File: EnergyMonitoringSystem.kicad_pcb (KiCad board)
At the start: 4 copper layers, 0 parts

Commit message: pcb layout init
1. Pulled all items from schematics
2. Set board stackup and constraints
3. Create polygon pours for power and ground
4. Created isolated ground and power
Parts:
- added C201: 100n, Capacitor_SMD:C_0402_1005Metric, F.Cu at (99.7, 53.1)
- added C202: 100n, Capacitor_SMD:C_0402_1005Metric, F.Cu at (95.7, 48.9)
- added C203: 10u, Capacitor_SMD:C_0603_1608Metric, F.Cu at (108.0, 58.0)
- added C204: 10u, Capacitor_SMD:C_0603_1608Metric, F.Cu at (109.4, 52.6)
- added C301: 1u, Capacitor_SMD:C_0402_1005Metric, F.Cu at (115.2, 91.7)
- added C302: 1u, Capacitor_SMD:C_0402_1005Metric, F.Cu at (108.7, 93.0)
- added C303: 10u, Capacitor_SMD:C_0603_1608Metric, F.Cu at (97.1, 72.0)
- added C304: 47u, Capacitor_SMD:C_0603_1608Metric, F.Cu at (100.8, 72.0)
- added C305: 47u, Capacitor_SMD:C_0603_1608Metric, F.Cu at (101.3, 68.0)
- added C306: 10u, EMS:10SVPS10M, F.Cu at (125.5, 96.5)
- added C307: 10u, Capacitor_SMD:C_0603_1608Metric, F.Cu at (115.2, 67.8)
- added C308: 47u, Capacitor_SMD:C_0603_1608Metric, F.Cu at (109.9, 72.0)
- added C309: 47u, Capacitor_SMD:C_0603_1608Metric, F.Cu at (111.7, 63.2)
- added C310: 10u, EMS:10SVPS10M, F.Cu at (119.5, 104.5)
- added C401: 100n, Capacitor_SMD:C_0402_1005Metric, F.Cu at (132.8, 47.0)
- added C402: 100n, Capacitor_SMD:C_0402_1005Metric, F.Cu at (161.5, 65.2)
- added C403: 100n, Capacitor_SMD:C_0402_1005Metric, F.Cu at (157.0, 73.5)
- added C404: 100n, Capacitor_SMD:C_0402_1005Metric, F.Cu at (153.0, 70.0)
- added C405: 100n, Capacitor_SMD:C_0402_1005Metric, F.Cu at (146.2, 109.7)
- added C406: 100n, Capacitor_SMD:C_0402_1005Metric, F.Cu at (146.2, 113.2)
- added C407: 100n, Capacitor_SMD:C_0402_1005Metric, F.Cu at (157.0, 84.5)
- added C408: 2u2, Capacitor_SMD:C_0402_1005Metric, F.Cu at (155.0, 135.5)
- added C409: 100n, Capacitor_SMD:C_0402_1005Metric, F.Cu at (157.0, 135.5)
- added C410: 1u, Capacitor_SMD:C_0402_1005Metric, F.Cu at (154.5, 88.0)
- added C411: 1u, Capacitor_SMD:C_0402_1005Metric, F.Cu at (158.5, 91.0)
- added C412: 10n, Capacitor_SMD:C_0402_1005Metric, F.Cu at (154.5, 92.0)
- added C413: 100n, Capacitor_SMD:C_0402_1005Metric, F.Cu at (136.0, 136.5)
- added C414: 100n, Capacitor_SMD:C_0402_1005Metric, F.Cu at (142.0, 75.5)
- added C415: 100n, Capacitor_SMD:C_0402_1005Metric, F.Cu at (142.0, 82.5)
- added C416: 10u, Capacitor_SMD:C_0603_1608Metric, F.Cu at (139.0, 82.8)
- added C417: 6p8, Capacitor_SMD:C_0402_1005Metric, F.Cu at (151.0, 59.5)
- added C418: 5p6, Capacitor_SMD:C_0402_1005Metric, F.Cu at (159.3, 69.8)
- added C419: 100n, Capacitor_SMD:C_0402_1005Metric, F.Cu at (167.0, 81.5)
- added C420: 6p8, Capacitor_SMD:C_0402_1005Metric, F.Cu at (147.0, 63.5)
- added C421: 5p6, Capacitor_SMD:C_0402_1005Metric, F.Cu at (156.3, 65.5)
- added C501: 10p, Capacitor_SMD:C_0603_1608Metric, F.Cu at (72.5, 55.3)
- added C502: 6800p, Capacitor_SMD:C_0603_1608Metric, F.Cu at (75.5, 57.2)
- added C503: 10p, Capacitor_SMD:C_0603_1608Metric, F.Cu at (72.5, 58.8)
- added C504: 10p, Capacitor_SMD:C_0603_1608Metric, F.Cu at (72.2, 80.7)
- added C505: 6800p, Capacitor_SMD:C_0603_1608Metric, F.Cu at (74.8, 83.5)
- added C506: 10p, Capacitor_SMD:C_0603_1608Metric, F.Cu at (72.2, 85.7)
- added C507: 10p, Capacitor_SMD:C_0603_1608Metric, F.Cu at (72.2, 111.7)
- added C508: 6800p, Capacitor_SMD:C_0603_1608Metric, F.Cu at (74.5, 114.7)
- added C509: 10p, Capacitor_SMD:C_0603_1608Metric, F.Cu at (72.2, 116.7)
- added C510: 220n, Capacitor_SMD:C_0402_1005Metric, F.Cu at (93.8, 87.7)
- added C511: 1u, Capacitor_SMD:C_0402_1005Metric, F.Cu at (93.1, 89.7)
- added C512: 1u, Capacitor_SMD:C_0402_1005Metric, F.Cu at (100.3, 90.7)
- added C513: 10p, Capacitor_SMD:C_0603_1608Metric, F.Cu at (93.6, 84.9)
- added C514: 10p, Capacitor_SMD:C_0603_1608Metric, F.Cu at (89.2, 110.5)
- added C515: 6800p, Capacitor_SMD:C_0603_1608Metric, F.Cu at (92.8, 110.5)
- added C516: 10p, Capacitor_SMD:C_0603_1608Metric, F.Cu at (108.5, 110.5)
- added C517: 6800p, Capacitor_SMD:C_0603_1608Metric, F.Cu at (112.0, 110.5)
- added C518: 10p, Capacitor_SMD:C_0603_1608Metric, F.Cu at (127.0, 110.5)
- added C519: 6800p, Capacitor_SMD:C_0603_1608Metric, F.Cu at (130.7, 110.5)
- added C601: 100n, Capacitor_SMD:C_0402_1005Metric, F.Cu at (167.5, 128.2)
- added C602: 100n, Capacitor_SMD:C_0402_1005Metric, F.Cu at (164.8, 128.0)
- added C603: 10u, Capacitor_SMD:C_0603_1608Metric, F.Cu at (169.0, 96.0)
- added C604: 0.1u, Capacitor_SMD:C_0402_1005Metric, F.Cu at (166.0, 102.5)
- added C605: 0.1u, Capacitor_SMD:C_0402_1005Metric, F.Cu at (183.0, 116.5)
- added C606: 10u, Capacitor_SMD:C_0603_1608Metric, F.Cu at (181.0, 112.0)
- added C607: 10u, Capacitor_SMD:C_0603_1608Metric, F.Cu at (169.0, 107.0)
- added C608: 0.1u, Capacitor_SMD:C_0402_1005Metric, F.Cu at (163.0, 97.5)
- added C609: 0.1u, Capacitor_SMD:C_0402_1005Metric, F.Cu at (186.0, 111.5)
- added D201: BAT30KFILM, EMS:BAT30KFILM, F.Cu at (96.6, 46.2)
- added D202: ESDA7P60-1U1M, EMS:ESDA7P60-1U1M, F.Cu at (92.3, 46.7)
- added D401: ESDALC6V1-1M2, EMS:ESDALC6V11M2, F.Cu at (152.9, 51.8)
- added D402: ESDALC6V1-1M2, EMS:ESDALC6V11M2, F.Cu at (135.5, 51.0)
- added D403: PESD3V3L1BA,115, EMS:PESD3V3L1BA_115-SOD-323-2, F.Cu at (168.5, 58.5)
- added D404: PESD3V3L1BA,115, EMS:PESD3V3L1BA_115-SOD-323-2, F.Cu at (179.7, 57.3)
- added D405: PESD3V3L1BA,115, EMS:PESD3V3L1BA_115-SOD-323-2, F.Cu at (180.0, 63.3)
- added D406: PESD3V3L1BA,115, EMS:PESD3V3L1BA_115-SOD-323-2, F.Cu at (183.7, 60.8)
- added D407: PESD3V3L1BA,115, EMS:PESD3V3L1BA_115-SOD-323-2, F.Cu at (183.7, 54.6)
- added D408: LED_RAGB, LED_SMD:LED_Kingbright_APFA3010_3x1.5mm_Horizontal, F.Cu at (169.0, 78.5)
- added FB601: FerriteBead, EMS:BLM15HD182SN1D, F.Cu at (180.0, 118.4)
- added FB602: FerriteBead, EMS:BLM15HD182SN1D, F.Cu at (187.0, 106.4)
- added J201: USB_C_Receptacle_USB2.0_16P, Connector_USB:USB_C_Receptacle_GCT_USB4105-xx-A_16P_TopMnt_Horizontal, F.Cu at (103.5, 41.3)
- added J202: Screw_Terminal_01x02, TerminalBlock_Phoenix:TerminalBlock_Phoenix_MKDS-1,5-2-5.08_1x02_P5.08mm_Horizontal, F.Cu at (121.0, 42.1)
- added J401: Conn_02x05_Counter_Clockwise, EMS:62701021621, F.Cu at (172.7, 55.9)
- added J402: Conn_02x05_Counter_Clockwise, EMS:62701021621, F.Cu at (152.7, 120.9)
- added J403: Conn_02x08_Counter_Clockwise, Connector_PinHeader_2.54mm:PinHeader_2x10_P2.54mm_Vertical, F.Cu at (141.2, 101.0)
- added J501: Screw_Terminal_01x02, TerminalBlock_Phoenix:TerminalBlock_Phoenix_MKDS-1,5-2-5.08_1x02_P5.08mm_Horizontal, F.Cu at (35.5, 56.9)
- added J502: Screw_Terminal_01x02, TerminalBlock_Phoenix:TerminalBlock_Phoenix_MKDS-1,5-2-5.08_1x02_P5.08mm_Horizontal, F.Cu at (35.5, 85.8)
- added J503: Screw_Terminal_01x02, TerminalBlock_Phoenix:TerminalBlock_Phoenix_MKDS-1,5-2-5.08_1x02_P5.08mm_Horizontal, F.Cu at (35.5, 114.4)
- added J504: Screw_Terminal_01x02, TerminalBlock_Phoenix:TerminalBlock_Phoenix_MKDS-1,5-2-5.08_1x02_P5.08mm_Horizontal, F.Cu at (84.9, 144.0)
- added J505: Screw_Terminal_01x02, TerminalBlock_Phoenix:TerminalBlock_Phoenix_MKDS-1,5-2-5.08_1x02_P5.08mm_Horizontal, F.Cu at (104.5, 144.0)
- added J506: Screw_Terminal_01x02, TerminalBlock_Phoenix:TerminalBlock_Phoenix_MKDS-1,5-2-5.08_1x02_P5.08mm_Horizontal, F.Cu at (123.9, 144.0)
- added J601: DM3AT-SF-PEJM5_40_, EMS:DM3ATSFPEJM540, F.Cu at (169.6, 133.0)
- added J602: Screw_Terminal_01x03, TerminalBlock_Phoenix:TerminalBlock_Phoenix_MKDS-1,5-3-5.08_1x03_P5.08mm_Horizontal, F.Cu at (195.0, 110.0)
- added L301: 2u2, Inductor_SMD:L_0603_1608Metric, F.Cu at (93.8, 67.5)
- added L302: 10u, Inductor_SMD:L_0805_2012Metric, F.Cu at (93.8, 63.7)
- added L303: 2u2, Inductor_SMD:L_0603_1608Metric, F.Cu at (108.0, 68.0)
- added L304: 10u, Inductor_SMD:L_0805_2012Metric, F.Cu at (108.0, 64.2)
- added L401: 10n, Inductor_SMD:L_0603_1608Metric, F.Cu at (158.2, 88.0)
- added Q201: STL6N3LLH6, EMS:STL6N3LLH6, F.Cu at (101.1, 54.9)
- added R201: 10k, Resistor_SMD:R_0603_1608Metric, F.Cu at (103.4, 48.1)
- added R202: 120R, Resistor_SMD:R_0402_1005Metric, F.Cu at (112.1, 56.3)
- added R203: 2k7, Resistor_SMD:R_0603_1608Metric, F.Cu at (103.4, 51.8)
- added R301: 100k, Resistor_SMD:R_0603_1608Metric, F.Cu at (114.4, 88.2)
- added R302: 100k, Resistor_SMD:R_0603_1608Metric, F.Cu at (115.3, 70.8)
- added R401: 49R9, Resistor_SMD:R_0402_1005Metric, F.Cu at (171.5, 49.9)
- added R402: 49R9, Resistor_SMD:R_0402_1005Metric, F.Cu at (175.2, 49.9)
- added R403: 49R9, Resistor_SMD:R_0402_1005Metric, F.Cu at (171.2, 46.7)
- added R404: 49R9, Resistor_SMD:R_0402_1005Metric, F.Cu at (175.2, 46.7)
- added R405: 10k, Resistor_SMD:R_0603_1608Metric, F.Cu at (149.4, 46.2)
- added R406: 47k, Resistor_SMD:R_0603_1608Metric, F.Cu at (136.0, 140.8)
- added R407: 47k, Resistor_SMD:R_0603_1608Metric, F.Cu at (157.0, 141.2)
- added R408: 1k, Resistor_SMD:R_0603_1608Metric, F.Cu at (165.1, 80.0)
- added R409: 1k, Resistor_SMD:R_0603_1608Metric, F.Cu at (165.1, 78.5)
- added R410: 1k, Resistor_SMD:R_0603_1608Metric, F.Cu at (165.1, 77.0)
- added R501: 330k, Resistor_SMD:R_0805_2012Metric, F.Cu at (57.4, 54.5)
- added R502: 330k, Resistor_SMD:R_0805_2012Metric, F.Cu at (61.4, 54.5)
- added R503: 330k, Resistor_SMD:R_0805_2012Metric, F.Cu at (65.3, 54.5)
- added R504: 1k, Resistor_SMD:R_0603_1608Metric, F.Cu at (69.2, 54.5)
- added R505: R_Variable, EMS:B72220S0271K101, F.Cu at (52.0, 54.5)
- added R506: 750R, Resistor_SMD:R_0805_2012Metric, F.Cu at (65.2, 58.1)
- added R507: 1k, Resistor_SMD:R_0603_1608Metric, F.Cu at (69.2, 59.0)
- added R508: 330k, Resistor_SMD:R_0805_2012Metric, F.Cu at (57.1, 80.0)
- added R509: 330k, Resistor_SMD:R_0805_2012Metric, F.Cu at (61.1, 80.0)
- added R510: 330k, Resistor_SMD:R_0805_2012Metric, F.Cu at (65.1, 80.0)
- added R511: 1k, Resistor_SMD:R_0603_1608Metric, F.Cu at (68.9, 80.0)
- added R512: R_Variable, EMS:B72220S0271K101, F.Cu at (52.0, 82.5)
- added R513: 750R, Resistor_SMD:R_0805_2012Metric, F.Cu at (65.0, 84.1)
- added R514: 1k, Resistor_SMD:R_0603_1608Metric, F.Cu at (68.9, 85.0)
- added R515: 330k, Resistor_SMD:R_0805_2012Metric, F.Cu at (56.9, 111.0)
- added R516: 330k, Resistor_SMD:R_0805_2012Metric, F.Cu at (61.0, 111.0)
- added R517: 330k, Resistor_SMD:R_0805_2012Metric, F.Cu at (65.0, 111.0)
- added R518: 1k, Resistor_SMD:R_0603_1608Metric, F.Cu at (69.0, 111.0)
- added R519: R_Variable, EMS:B72220S0271K101, F.Cu at (52.0, 111.0)
- added R520: 750R, Resistor_SMD:R_0805_2012Metric, F.Cu at (64.8, 115.1)
- added R521: 1k, Resistor_SMD:R_0603_1608Metric, F.Cu at (69.0, 116.0)
- added R522: 33R, Resistor_SMD:R_0603_1608Metric, F.Cu at (94.4, 82.1)
- added R523: 33R, Resistor_SMD:R_0603_1608Metric, F.Cu at (96.3, 83.5)
- added R524: 7k15, Resistor_SMD:R_0603_1608Metric, F.Cu at (89.0, 134.5)
- added R525: 33R, Resistor_SMD:R_0603_1608Metric, F.Cu at (98.0, 83.5)
- added R526: 10k, Resistor_SMD:R_0603_1608Metric, F.Cu at (103.7, 82.7)
- added R527: 33R, Resistor_SMD:R_0603_1608Metric, F.Cu at (99.6, 83.5)
- added R528: 100k, Resistor_SMD:R_0603_1608Metric, F.Cu at (98.9, 86.0)
- added R529: 33R, Resistor_SMD:R_0603_1608Metric, F.Cu at (101.2, 83.5)
- added R530: 100k, Resistor_SMD:R_0603_1608Metric, F.Cu at (107.5, 86.0)
- added R531: 1k, Resistor_SMD:R_0603_1608Metric, F.Cu at (88.2, 131.6)
- added R532: 2k, Resistor_SMD:R_0603_1608Metric, F.Cu at (90.8, 114.0)
- added R533: 33R, Resistor_SMD:R_0603_1608Metric, F.Cu at (104.1, 89.8)
- added R534: 100k, Resistor_SMD:R_0603_1608Metric, F.Cu at (84.8, 133.6)
- added R535: 100k, Resistor_SMD:R_0603_1608Metric, F.Cu at (80.9, 128.5)
- added R536: 62k, Resistor_SMD:R_0603_1608Metric, F.Cu at (90.8, 117.2)
- added R537: 100k, Resistor_SMD:R_0603_1608Metric, F.Cu at (85.6, 130.8)
- added R538: 10k, Resistor_SMD:R_0603_1608Metric, F.Cu at (86.6, 117.2)
- added R539: 100k, Resistor_SMD:R_0603_1608Metric, F.Cu at (92.9, 129.0)
- added R540: 7k15, Resistor_SMD:R_0603_1608Metric, F.Cu at (103.7, 131.8)
- added R541: 1k, Resistor_SMD:R_0603_1608Metric, F.Cu at (108.2, 131.8)
- added R542: 2k, Resistor_SMD:R_0603_1608Metric, F.Cu at (110.1, 113.8)
- added R543: 100k, Resistor_SMD:R_0603_1608Metric, F.Cu at (104.5, 134.9)
- added R544: 100k, Resistor_SMD:R_0603_1608Metric, F.Cu at (103.7, 129.0)
- added R545: 62k, Resistor_SMD:R_0603_1608Metric, F.Cu at (110.1, 117.2)
- added R546: 100k, Resistor_SMD:R_0603_1608Metric, F.Cu at (108.3, 135.5)
- added R547: 10k, Resistor_SMD:R_0603_1608Metric, F.Cu at (103.6, 117.2)
- added R548: 100k, Resistor_SMD:R_0603_1608Metric, F.Cu at (110.9, 129.0)
- added R549: 7k15, Resistor_SMD:R_0603_1608Metric, F.Cu at (123.2, 131.8)
- added R550: 1k, Resistor_SMD:R_0603_1608Metric, F.Cu at (128.2, 131.8)
- added R551: 2k, Resistor_SMD:R_0603_1608Metric, F.Cu at (128.7, 113.5)
- added R552: 100k, Resistor_SMD:R_0603_1608Metric, F.Cu at (123.5, 135.1)
- added R553: 100k, Resistor_SMD:R_0603_1608Metric, F.Cu at (123.1, 129.0)
- added R554: 62k, Resistor_SMD:R_0603_1608Metric, F.Cu at (129.3, 117.5)
- added R555: 100k, Resistor_SMD:R_0603_1608Metric, F.Cu at (128.3, 136.0)
- added R556: 10k, Resistor_SMD:R_0603_1608Metric, F.Cu at (123.3, 117.5)
- added R557: 100k, Resistor_SMD:R_0603_1608Metric, F.Cu at (130.8, 129.0)
- added R601: 120R, Resistor_SMD:R_0402_1005Metric, F.Cu at (183.0, 121.0)
- added SW401: SW_Push, Button_Switch_SMD:SW_SPST_CK_RS282G05A3, F.Cu at (139.0, 47.0)
- added SW402: SW_Push, Button_Switch_SMD:SW_SPST_CK_RS282G05A3, F.Cu at (155.9, 47.0)
- added TP201: TestPoint, EMS:5000, F.Cu at (85.0, 56.0)
- added TP202: TestPoint, EMS:5000, F.Cu at (85.0, 64.0)
- added TP301: TestPoint, EMS:5000, F.Cu at (64.8, 145.0)
- added TP302: TestPoint, EMS:5000, F.Cu at (64.8, 131.8)
- added TP303: TestPoint, EMS:5000, F.Cu at (64.8, 135.5)
- added TP304: TestPoint, EMS:5000, F.Cu at (64.8, 139.2)
- added TP601: TestPoint, EMS:5000, F.Cu at (187.0, 92.0)
- added TP602: TestPoint, EMS:5000, F.Cu at (182.0, 130.0)
- added TP603: TestPoint, EMS:5000, F.Cu at (173.0, 92.0)
- added U201: USBLC6-2P6, EMS:USBLC62P6-SOT666-6, F.Cu at (108.1, 49.1)
- added U202: STEF05SGR, EMS:STEF05SGR-TSOT23-8L, F.Cu at (108.6, 55.4)
- added U203: TCPP01-M12, EMS:TCPP01-M12-QFN-12L, F.Cu at (98.7, 50.2)
- added U301: LDLN025M12R, EMS:LDLN025M12R-SOT-23-5, F.Cu at (112.2, 91.2)
- added U302: ST1PS02CQTR, EMS:ST1PS02CQTR, F.Cu at (97.6, 67.5)
- added U303: ST1PS02CQTR, EMS:ST1PS02CQTR, F.Cu at (111.7, 67.6)
- added U304: LM2664M6_NOPB, EMS:LM2664M6_NOPB-SOT-23-6, F.Cu at (125.8, 102.0)
- added U401: STM32F103RGT6, EMS:STM32F103RGT6-LQFP-64, F.Cu at (149.5, 78.8)
- added U402: BLUENRG-M2SA, EMS:BLUENRG-M2SA, F.Cu at (146.5, 145.2)
- added U501: ADS131M08IRSNR, EMS:ADS131M08IPBS-WQFN-A, F.Cu at (96.6, 91.2)
- added U502: TSV914AIDR, EMS:TSV914AIDR-SOIC-14, F.Cu at (87.5, 123.4)
- added U503: TSV914AIDR, EMS:TSV914AIDR-SOIC-14, F.Cu at (106.8, 123.4)
- added U504: TSV914AIDR, EMS:TSV914AIDR-SOIC-14, F.Cu at (126.2, 123.5)
- added U601: EMIF06-MSD02N16, EMS:EMIF06-MSD02N16, F.Cu at (160.3, 122.2)
- added U602: ADM2565EBRNZ, EMS:ADM2565EBRNZ-SOIC-28, F.Cu at (178.6, 103.2)
- added Y401: 16MHz, Crystal:Crystal_SMD_3225-4Pin_3.2x2.5mm, F.Cu at (151.1, 63.1)
- added Y402: 32.768KHz, Crystal:Crystal_SMD_3215-2Pin_3.2x1.5mm, F.Cu at (157.0, 67.5)
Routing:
- added copper zone on In3.Cu, net +DCDC_1
- added copper zone on In3.Cu, net +V_ISO
- added copper zone on In1.Cu, net GND
- added copper zone on In4.Cu, net GND
- added copper zone on In1.Cu, net GND2
- added copper zone on In4.Cu, net GND2
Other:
- board outline added: 170 x 117 mm
- copper layers 4 -> 6

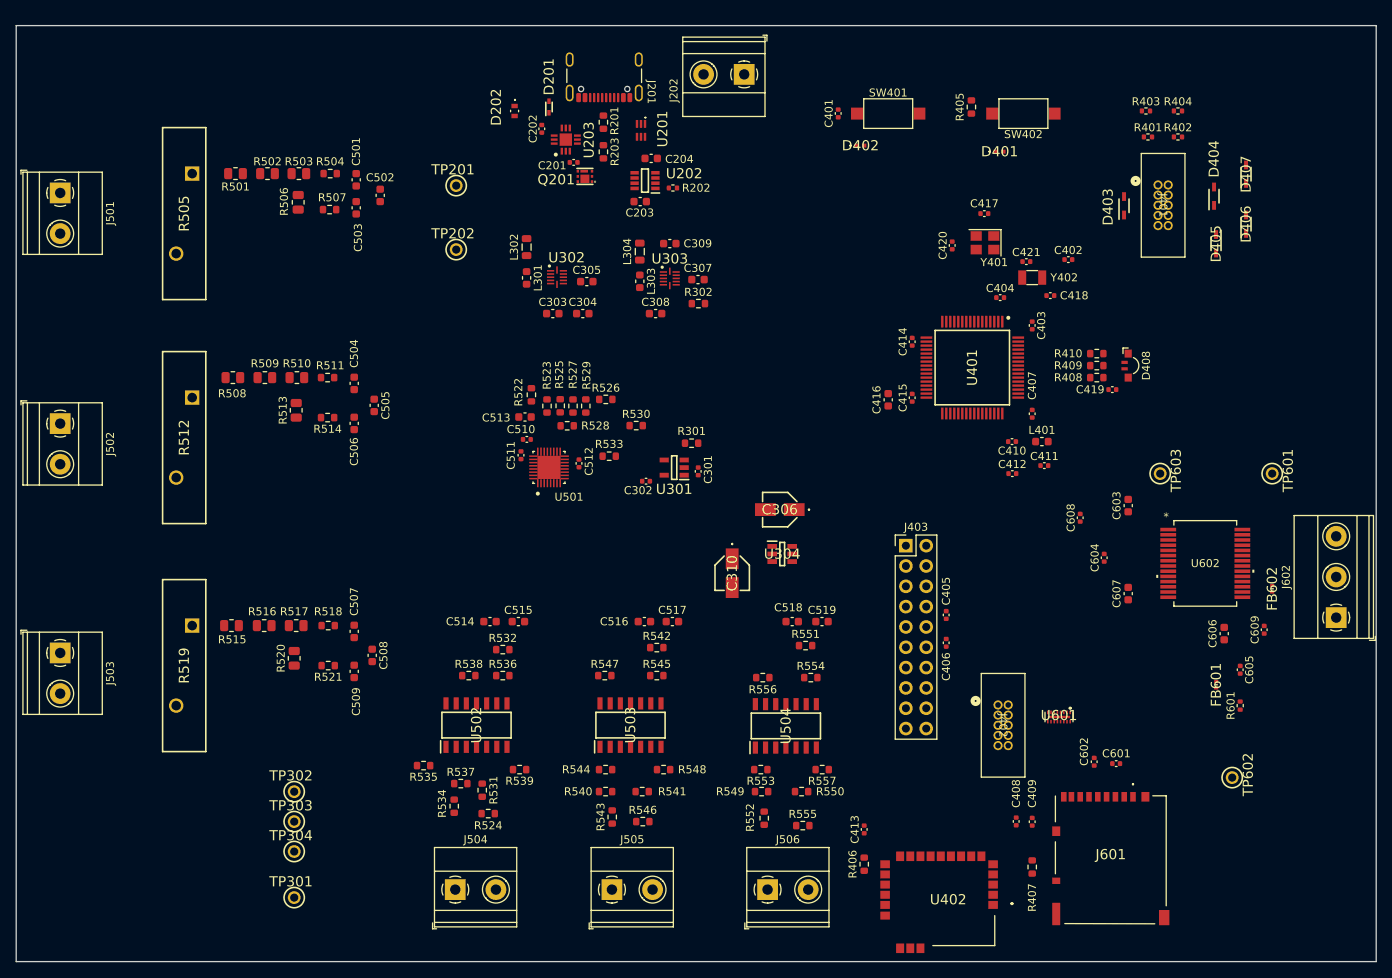
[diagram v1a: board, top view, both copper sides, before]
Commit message: routed board power supply
1. USB
2. LDO for DCDC_1 and DCDC_2
3. LDO for +1V2
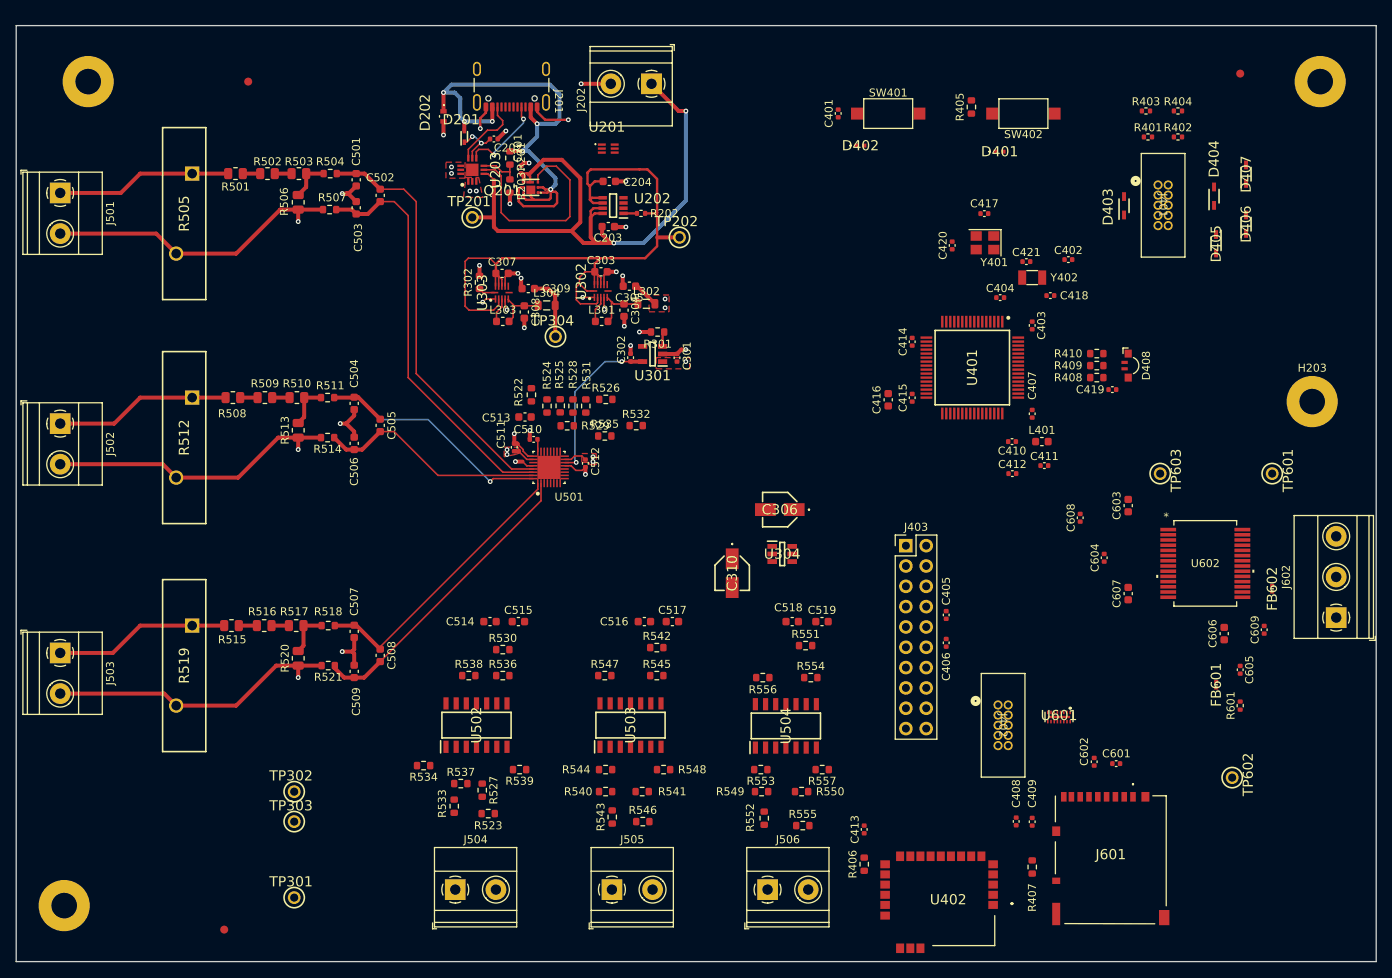
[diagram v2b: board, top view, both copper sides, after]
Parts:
- added FM201: Fiducial, Fiducial:Fiducial_1mm_Mask2mm, F.Cu at (59.0, 43.0)
- added FM202: Fiducial, Fiducial:Fiducial_1mm_Mask2mm, F.Cu at (183.0, 42.0)
- added FM203: Fiducial, Fiducial:Fiducial_1mm_Mask2mm, F.Cu at (56.0, 149.0)
- added H201: MountingHole_Pad, MountingHole:MountingHole_3.2mm_M3_Pad, F.Cu at (39.0, 43.0)
- added H202: MountingHole_Pad, MountingHole:MountingHole_3.2mm_M3_Pad, F.Cu at (193.0, 43.0)
- added H203: MountingHole_Pad, MountingHole:MountingHole_3.2mm_M3_Pad, F.Cu at (192.0, 83.0)
- added H204: MountingHole_Pad, MountingHole:MountingHole_3.2mm_M3_Pad, F.Cu at (36.0, 146.0)
- moved TP304 72.2 mm to (97.4, 74.9)
- moved TP202 28.0 mm to (112.9, 62.5)
- moved R302 27.5 mm to (87.9, 68.1), turned to 90 degrees
- moved C307 24.5 mm to (90.7, 67.0)
- moved U303 21.1 mm to (90.7, 69.4), turned to 90 degrees
- moved C309 18.6 mm to (94.0, 68.9)
- moved L303 17.8 mm to (90.8, 73.0), turned to 0 degrees
- moved L302 16.6 mm to (108.8, 70.8), turned to 0 degrees
- moved C308 16.4 mm to (93.5, 71.8), turned to -90 degrees
- moved C302 15.6 mm to (106.8, 77.5), turned to 90 degrees
- moved R301 14.5 mm to (110.2, 74.3), turned to 0 degrees
- moved U301 14.5 mm to (109.5, 77.0)
- moved C301 14.4 mm to (112.6, 77.5)
- moved L304 13.4 mm to (96.3, 71.0), turned to 0 degrees
- moved R201 12.5 mm to (91.7, 52.5)
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- renumbered R524 to R523, R523 to R524, R531 to R527, R527 to R528, R528 to R529, R532 to R530, R529 to R531, R530 to R532, R534 to R533, R535 to R534, R533 to R535
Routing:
- net GND: track 0.00 -> 181.1 mm, vias 0 -> 37
- net +5V: track 0.00 -> 92.0 mm
- net +5V_EXT: track 0.00 -> 83.1 mm, vias 0 -> 2
- net +VBUSc: track 0.00 -> 71.1 mm, vias 0 -> 6
- net /ADC/V_Phase_A_P: track 0.00 -> 52.4 mm
- net /ADC/V_Phase_A_N: track 0.00 -> 51.4 mm
- net /ADC/V_Phase_C_N: track 0.00 -> 37.9 mm
- net /ADC/V_Phase_C_P: track 0.00 -> 35.8 mm
- net /ADC/V_Phase_B_P: track 0.00 -> 29.4 mm, vias 0 -> 1
- net /ADC/V_Phase_B_N: track 0.00 -> 28.7 mm
- net /USB/PD_GATE: track 0.00 -> 26.9 mm
- net Net-(J502-Pin_1): track 0.00 -> 22.0 mm
- net Net-(J501-Pin_1): track 0.00 -> 22.0 mm
- net Net-(J503-Pin_1): track 0.00 -> 21.9 mm
- net +1V2: track 0.00 -> 20.4 mm, vias 0 -> 2
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- added copper zone on F.Cu, net +DCDC_1
- added copper zone on F.Cu, net GND

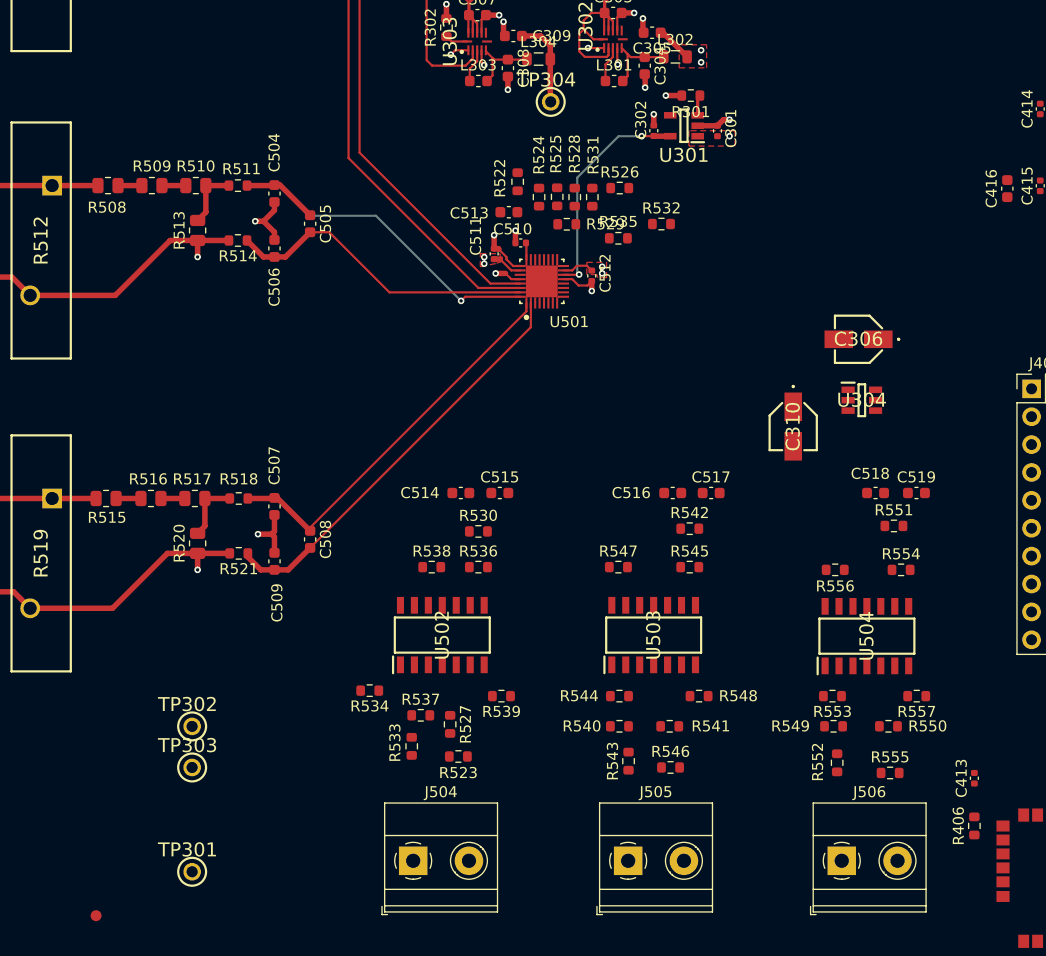
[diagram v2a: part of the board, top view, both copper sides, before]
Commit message: routing of CTs complete
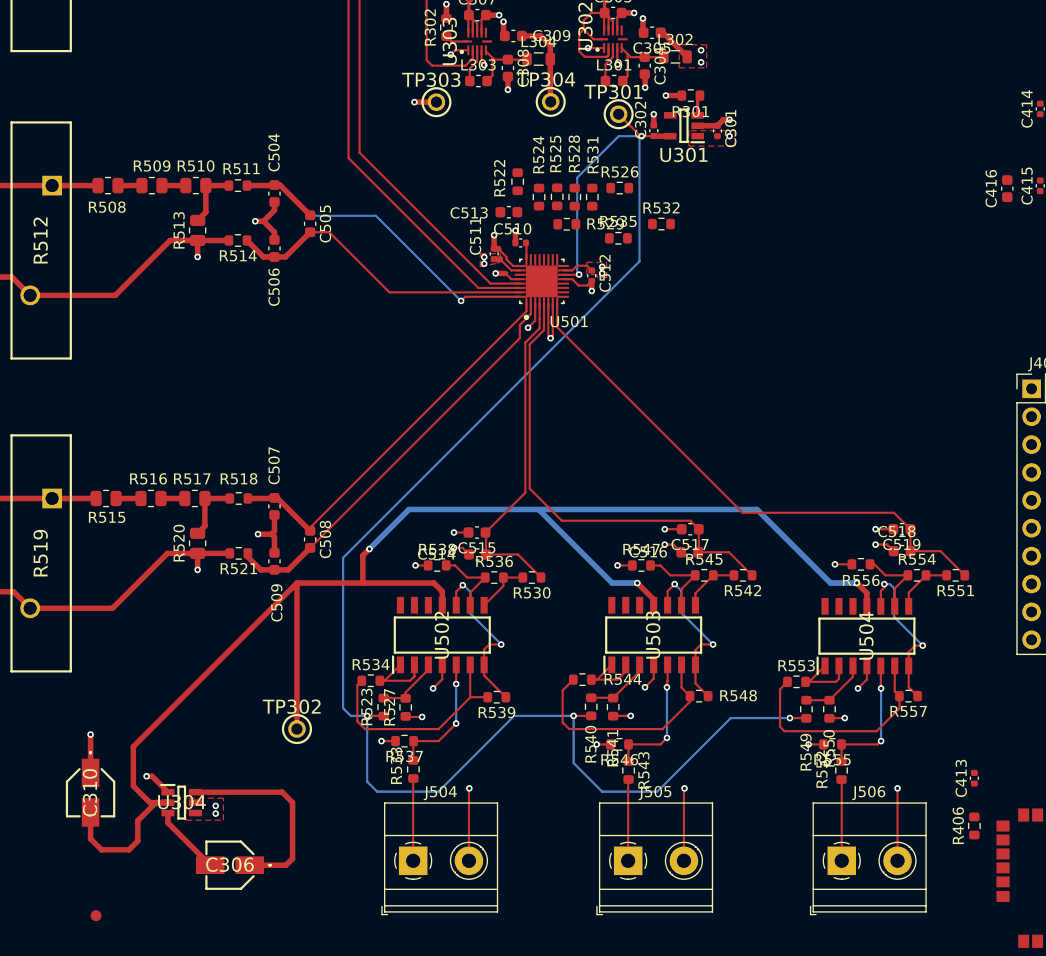
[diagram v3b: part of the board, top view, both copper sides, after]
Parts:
- moved TP301 79.2 mm to (103.6, 76.0)
- moved C306 74.6 mm to (68.2, 144.4)
- moved C310 72.2 mm to (55.5, 137.8)
- moved U304 72.0 mm to (63.8, 138.7)
- moved TP303 64.6 mm to (87.0, 74.9)
- moved TP302 9.55 mm to (74.3, 132.0)
- moved R523 8.15 mm to (82.2, 130.0), turned to -90 degrees
- moved R551 7.20 mm to (134.3, 118.0), turned to 180 degrees
- moved R542 6.45 mm to (114.9, 118.0), turned to 180 degrees
- moved R530 6.43 mm to (95.7, 118.2), turned to 180 degrees
- moved R555 5.86 mm to (123.1, 133.4), turned to 180 degrees
- moved C518 5.83 mm to (129.4, 115.8)
- moved C514 5.80 mm to (90.8, 116.1)
- moved C516 5.62 mm to (110.1, 115.9)
- moved R550 5.59 mm to (122.8, 130.2), turned to 90 degrees
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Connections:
- R534 pad 2: /ADC/VB_REF -> /ADC/VB_REF_A
- R539 pad 1: /ADC/LS_REF -> /ADC/LS_REF_A
- R544 pad 2: /ADC/VB_REF -> /ADC/VB_REF_B
- R548 pad 1: /ADC/LS_REF -> /ADC/LS_REF_B
- R553 pad 2: /ADC/VB_REF -> /ADC/VB_REF_C
- R557 pad 1: /ADC/LS_REF -> /ADC/LS_REF_C
- U502 pad 1: /ADC/VB_REF -> /ADC/VB_REF_A
- U502 pad 10: /ADC/LS_REF -> /ADC/LS_REF_A
- U502 pad 2: /ADC/VB_REF -> /ADC/VB_REF_A
- U502 pad 7: /ADC/LS_REF -> /ADC/LS_REF_A
- U503 pad 1: /ADC/VB_REF -> /ADC/VB_REF_B
- U503 pad 10: /ADC/LS_REF -> /ADC/LS_REF_B
- U503 pad 2: /ADC/VB_REF -> /ADC/VB_REF_B
- U503 pad 7: /ADC/LS_REF -> /ADC/LS_REF_B
- U504 pad 1: /ADC/VB_REF -> /ADC/VB_REF_C
- U504 pad 10: /ADC/LS_REF -> /ADC/LS_REF_C
- U504 pad 2: /ADC/VB_REF -> /ADC/VB_REF_C
- U504 pad 7: /ADC/LS_REF -> /ADC/LS_REF_C
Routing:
- net -DCDC_1: track 0.00 -> 138.2 mm, vias 0 -> 3
- net +1V2: track 20.4 -> 149.7 mm, vias 2 -> 5
- net GND: track 181.1 -> 238.3 mm, vias 37 -> 59
- net /ADC/I_Phase_C_P: track 0.00 -> 49.9 mm
- net /ADC/I_Phase_B_P: track 0.00 -> 42.3 mm
- net /ADC/I_Phase_A_P: track 0.00 -> 30.8 mm
- net Net-(U503--INB): track 0.00 -> 20.9 mm
- net Net-(U504--INB): track 0.00 -> 20.3 mm
- net Net-(U502--INB): track 0.00 -> 20.2 mm
- net /VR/CHRG_CAP+: track 0.00 -> 18.5 mm
- net /ADC/LS_REF_A: track 0.00 -> 15.9 mm, vias 0 -> 2
- net /ADC/LS_REF_B: track 0.00 -> 15.6 mm, vias 0 -> 2
- net /ADC/LS_REF_C: track 0.00 -> 15.4 mm, vias 0 -> 2
- net Net-(U504-+INB): track 0.00 -> 12.1 mm, vias 0 -> 2
- net Net-(U503-+INB): track 0.00 -> 12.0 mm, vias 0 -> 2
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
